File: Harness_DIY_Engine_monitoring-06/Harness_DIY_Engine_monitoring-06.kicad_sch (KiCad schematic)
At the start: 19 parts, among them J11 Conn_01x06, U1 Con_GT-150-12_M, U12 Con_GT-150-16_F, U14 Con_GT-150-16_M, U15 Sparkfun_OBD2_UART, U9 CADBed_DUAL

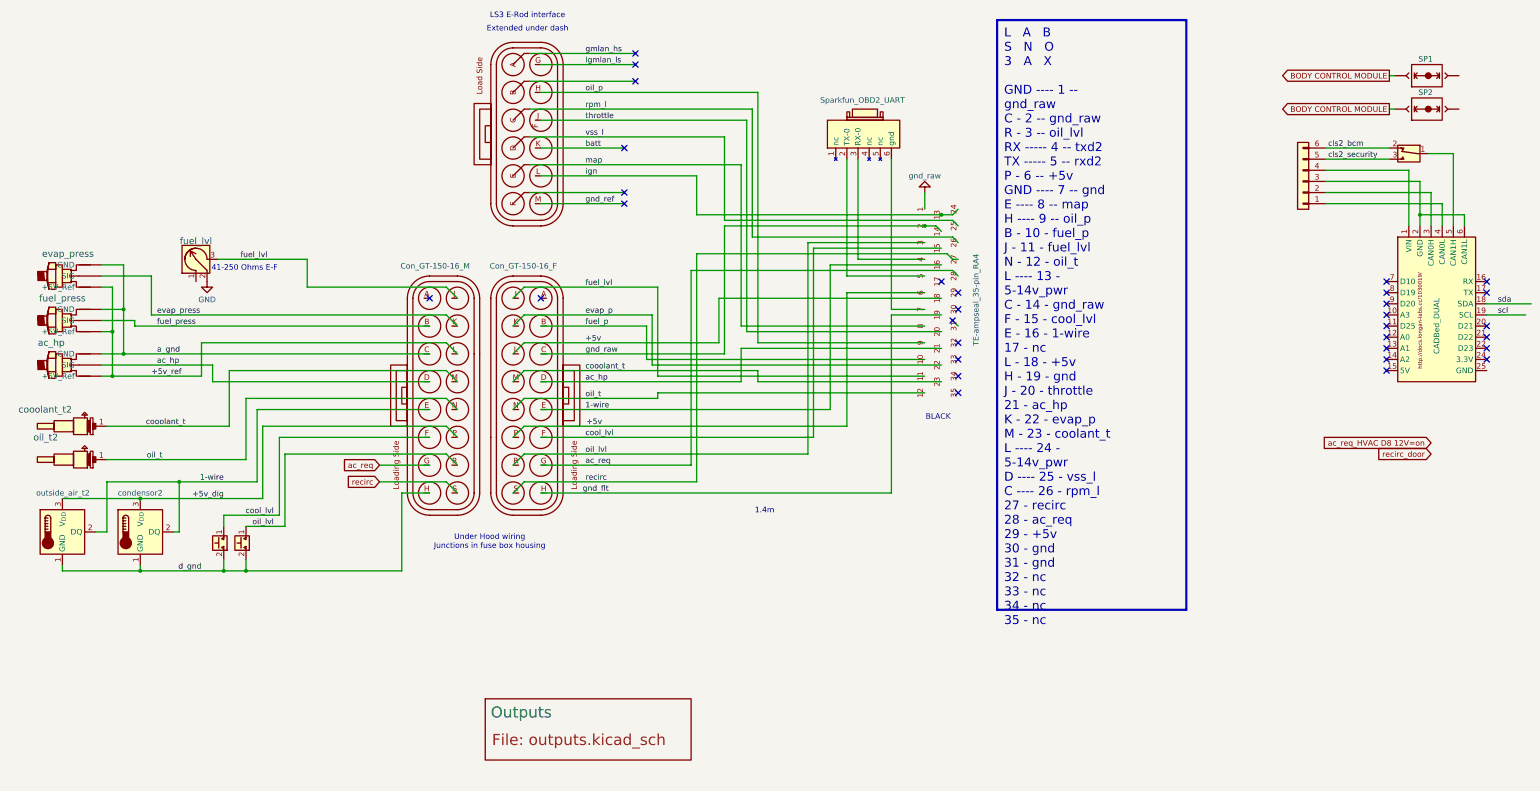
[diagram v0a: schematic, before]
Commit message: Many calibrations made
Still early days of getting code fixes and analog inputs calibrated
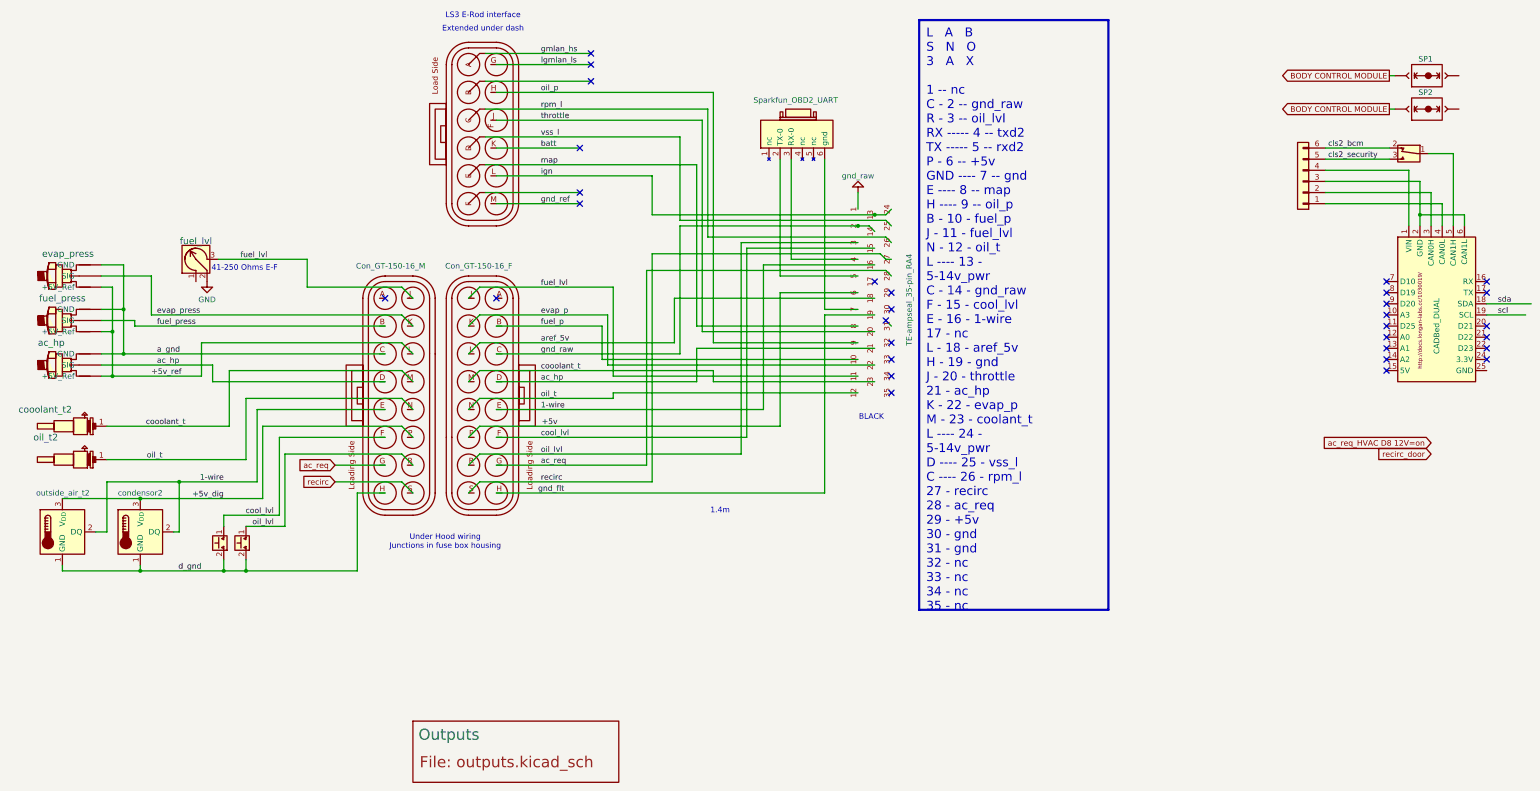
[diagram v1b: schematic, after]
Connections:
- net +5v: no longer TE-ampseal_35-pin_RA4.18, U12.L
- new net aref_5v: TE-ampseal_35-pin_RA4.18, U12.L
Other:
- moved on the sheet: TE-ampseal_35-pin_RA4
